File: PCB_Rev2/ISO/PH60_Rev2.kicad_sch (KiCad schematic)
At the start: 28 parts, among them J1 USB_C_Receptacle_USB2.0_16P, J2 Conn_01x02, U1 ME6211C33M5, U2 W25Q16JVSS, U3 RP2040, Y1 Crystal_GND24

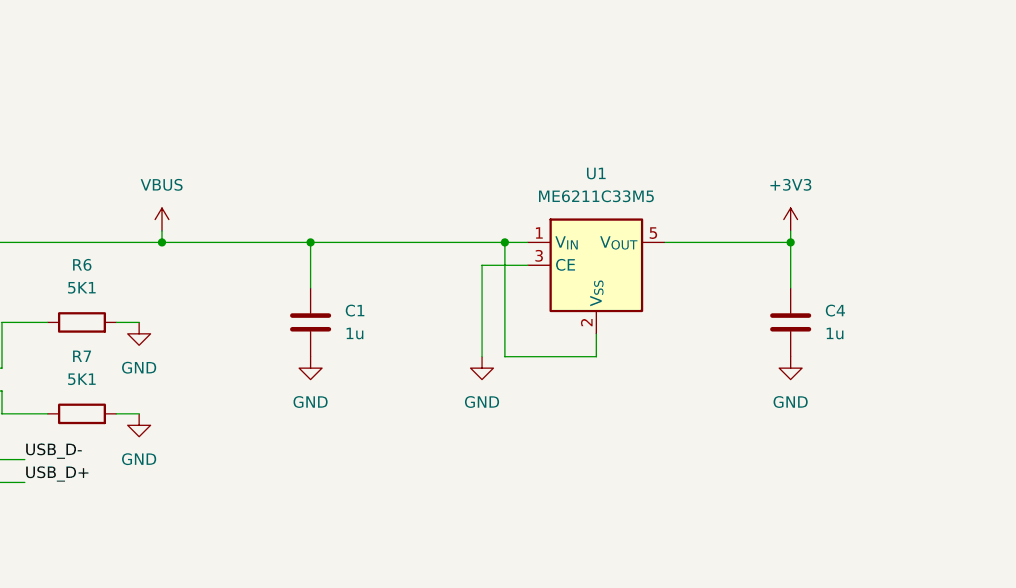
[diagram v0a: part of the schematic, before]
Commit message: Change LDO to XC6206
It must be work...
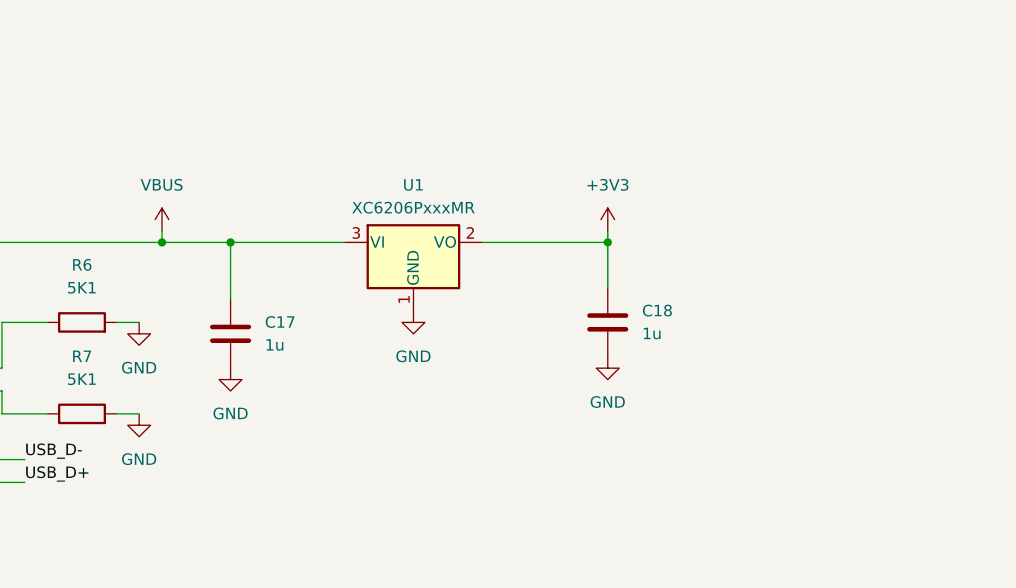
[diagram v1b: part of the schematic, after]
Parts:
- removed C1, C4: 1u, Capacitor_SMD:C_0402_1005Metric, symbol Device:C
- removed U1: ME6211C33M5, Package_TO_SOT_SMD:SOT-23-5, symbol Regulator_Linear:ME6211C33M5
- added C17, C18: 1u, Capacitor_SMD:C_0402_1005Metric, symbol Device:C
- added U1: XC6206PxxxMR, Package_TO_SOT_SMD:SOT-23-3, symbol Regulator_Linear:XC6206PxxxMR
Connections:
- net +3V3: now also C18.1, U1.2 (VO)
- net GND: now also C17.2, C18.2, U1.1 (GND)
- net VBUS: now also C17.1, U1.3 (VI)
